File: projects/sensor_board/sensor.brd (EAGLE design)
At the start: 90.2 x 95.9 mm, 49 parts, among them J1 504050-0791, J2 FH28-10S-0.5SH_05_, J3 504050-0791, J4 504050-1091, J5 504050-0791, J6 504050-0791, U1 NXP_FXAS21002CQR1_EDITEDNXP_F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, U2 HONEYWELL_HMC5983-TRHONEYWELL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, U3 DS1307N, U4 NXP_FXAS21002CQR1_EDITEDNXP_F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, U5 HONEYWELL_HMC5983-TRHONEYWELL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, U6 NXP_FXAS21002CQR1_EDITEDNXP_F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, U7 HONEYWELL_HMC5983-TRHONEYWELL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, Y1 ECS-.327-12.5-13X

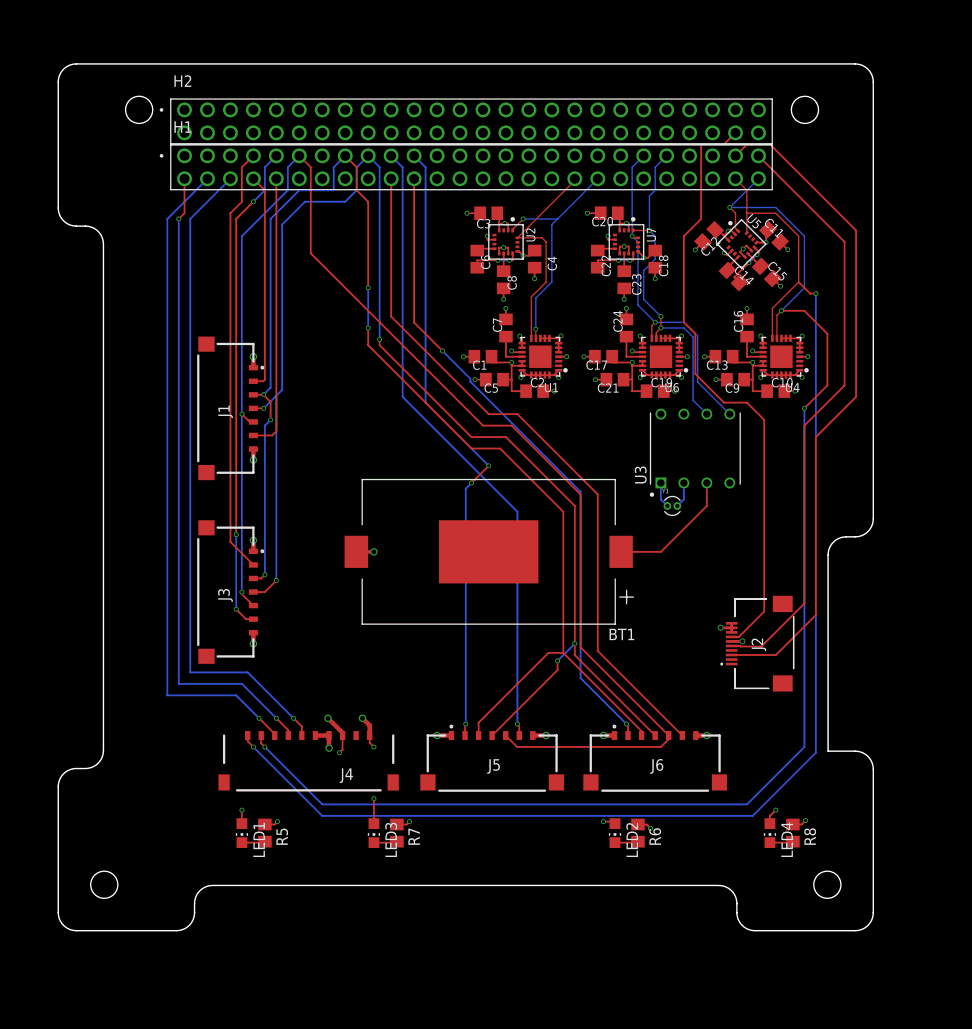
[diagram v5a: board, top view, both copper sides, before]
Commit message: sensor board updated
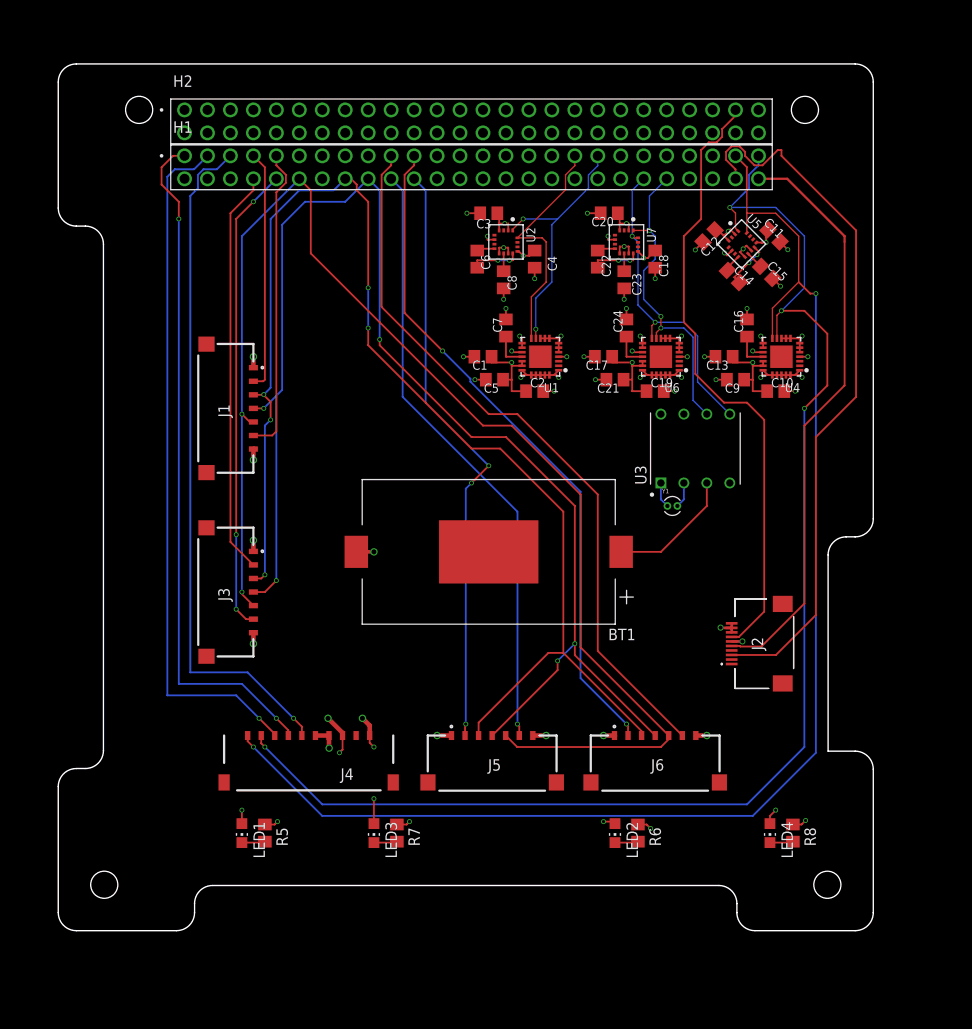
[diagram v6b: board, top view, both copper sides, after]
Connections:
- net 3V3_PDM10: now also H2.19; no longer H2.20
- net 3V3_PDM8: now also H2.17; no longer H2.18
- net 3V3_PDM9: now also H2.20; no longer H2.19
- net 5V_PDM5: now also H2.14; no longer H2.13
- net 5V_PDM6: now also H2.16; no longer H2.15
- net 5V_PDM7: now also H2.15; no longer H2.16
- net CHASSIS: now also H2.49; no longer H2.50
- net DTR: now also H1.5; no longer H1.6
- net GND: now also H2.10, H2.13, H2.18, H2.31; no longer H2.14, H2.17, H2.32, H2.9
- net I2C1_SCL: now also H1.44; no longer H1.43
- net I2C1_SDA: now also H1.42; no longer H1.41
- net I2C2_SCL: now also H1.37; no longer H1.38
- net I2C2_SDA: now also H1.35; no longer H1.36
- net I2C3_SCL: now also H1.51; no longer H1.52
- net I2C3_SDA: now also H1.49; no longer H1.50
- net SPI_EN_1: now also H1.7; no longer H1.8
- net SPI_EN_2: now also H1.8; no longer H1.7
- net SPI_EN_3: now also H1.22; no longer H1.21
- net SPI_EN_4: now also H1.21; no longer H1.22
- net SPI_MISO: now also H1.18; no longer H1.17
- net SPI_MOSI: now also H1.16; no longer H1.15
- net SPI_SCK: now also H1.12; no longer H1.11
- net SPI_SS_1: now also H1.9; no longer H1.10
- net SPI_SS_2: now also H1.10; no longer H1.9
- net SPI_SS_3: now also H1.20; no longer H1.19
- net SPI_SS_4: now also H1.19; no longer H1.20
- net UART2_RX: now also H1.4; no longer H1.3
- net UART2_TX: now also H1.2; no longer H1.1
- net UART3_RX: now also H1.52; no longer H1.51
- net UART3_TX: now also H1.50; no longer H1.49
- net UART8_RX: now also H1.3; no longer H1.4
- net UART8_TX: now also H1.1; no longer H1.2
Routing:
- net 3V3_PDM9: track 78.6 -> 104.5 mm
- net UART3_TX: track 73.3 -> 79.5 mm
- net SPI_MISO: track 153.4 -> 148.3 mm
- net SPI_SCK: track 156.8 -> 151.7 mm
- net UART8_TX: track 71.0 -> 75.8 mm
- net SPI_MOSI: track 149.0 -> 144.3 mm
- net UART8_RX: track 72.8 -> 76.6 mm
- net DTR: track 72.3 -> 75.7 mm
- net SPI_SS_1: track 30.7 -> 34.1 mm
- net SPI_SS_4: track 76.8 -> 80.2 mm
- net SPI_EN_4: track 71.4 -> 74.8 mm
- net 5V_PDM6: track 39.0 -> 41.8 mm
- net 5V_PDM7: track 21.0 -> 23.5 mm
- net SPI_EN_2: track 47.4 -> 44.8 mm
- net SPI_SS_3: track 70.0 -> 67.5 mm
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
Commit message: Update sensor.brd
Updated with fix to I2C lines
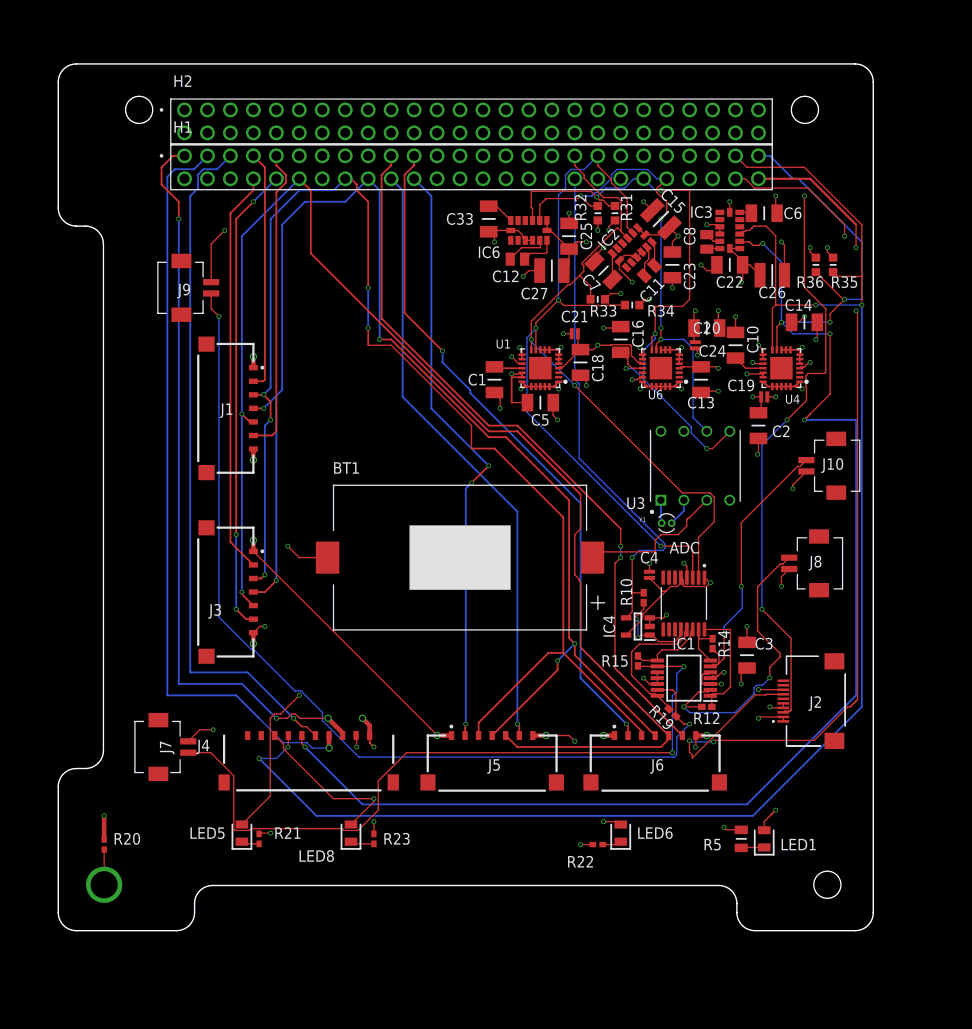
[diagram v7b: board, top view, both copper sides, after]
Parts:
- removed C17, C9: 1.0 uF, rcl:C0805
- removed LED2, LED3, LED4: (no value), led:CHIP-LED0805
- removed R6, R7, R8: (no value), rcl:R0805
- removed U2, U5, U7: HONEYWELL_HMC5983-TRHONEYWELL_HMC5983-TR_0_0, Honeywell - HMC5983-TR:HONEYWELL_HMC5983-TR_0
- added ADC: ADC128D818CIMT/NOPB, ADC128D818CIMT_NOPB:SOP65P640X120-16N
- added C25: C1206X104K5RAC3316, SamacSys_Parts:CAPC3316X98N
- added C26, C27: EMF325B7106KMHP, SamacSys_Parts:CAPC3225X270N
- added C33: C1206X475K3RACAUTO7210, SamacSys_Parts:CAPC3316X195N
- added IC1: TSX634AIYPT, SamacSys_Parts:SOP65P640X120-14N
- added IC2, IC3, IC6: LSM303DLHC, st-microelectronics:LGA-14
- added IC4: OPA991IDBVR, SamacSys_Parts:SOT95P280X145-5N
- added J10, J7, J8, J9: DF13A-2P-1.25H_21_, SamacSys_Parts:DF13A2P125H21
- added LED5, LED6, LED8: LG_R971-KN-1, SamacSys_Parts:LEDC2012X80N
- added R10, R12, R14, R15, R19: PTN0402Y1002BST1, SamacSys_Parts:RESC1106X84N
- added R20: PMR01ZZPJ000, SamacSys_Parts:RESC1005X35N
- added R21, R22, R23: CR0402-FX-1400GLF, SamacSys_Parts:RESC1005X40N
- added R31, R32, R33, R34, R35, R36: RS73G1JTTD4701B, SamacSys_Parts:RESC1608X55N
- BT1: device BA2032SM:BAT_BA2032SM -> BA2032SM_PAD_replace:BAT_BA2032SM
- C1: value 1.0 uF -> C1206X104K5RAC3316; device rcl:C0805 -> SamacSys_Parts:CAPC3316X98N
- C10, C13, C18, C2, C20, C3, C5: value 0.1 uF -> C1206X104K5RAC3316; device rcl:C0805 -> SamacSys_Parts:CAPC3316X98N
- C11, C12: value 0.1 uF -> C0805F224M5RACAUTO7210; device rcl:C0805 -> SamacSys_Parts:CAPC2012X140N
- C14, C22: value 0.22 uF -> C1206X104K5RAC3316; device rcl:C0805 -> SamacSys_Parts:CAPC3316X98N
- C15: value 4.7 uF -> EMF325B7106KMHP; device rcl:C0805 -> SamacSys_Parts:CAPC3225X270N
- C16: value 100 nF -> C1206X104K5RAC3316; device rcl:C0805 -> SamacSys_Parts:CAPC3316X98N
- C19, C21, C4: value 0.1 uF -> CGAEB1X7T0G105M050BC; device rcl:C0805 -> SamacSys_Parts:CAPC0611X68N
- C23: value 4.7 uF -> C1206X104K5RAC3316; device rcl:C0805 -> SamacSys_Parts:CAPC3316X98N
- C24: value 100 nF -> CGAEB1X7T0G105M050BC; device rcl:C0805 -> SamacSys_Parts:CAPC0611X68N
- C6: value 0.22 uF -> C1206X475K3RACAUTO7210; device rcl:C0805 -> SamacSys_Parts:CAPC3316X195N
- C7: value 100 nF -> C1206X475K3RACAUTO7210; device rcl:C0805 -> SamacSys_Parts:CAPC3316X195N
- C8: value 4.7 uF -> C0805F224M5RACAUTO7210; device rcl:C0805 -> SamacSys_Parts:CAPC2012X140N
- LED1: value (none) -> LH_R974-LP-1; device led:CHIP-LED0805 -> SamacSys_Parts:LEDC2012X90N
- R5: value (none) -> RN73H2ATTD75R0B25; device rcl:R0805 -> SamacSys_Parts:RESC2012X60N
- moved LED1 57.8 mm to (78.1, 10.2), turned to 90 degrees
- moved C3 56.6 mm to (76.2, 30.5), turned to 270 degrees
- moved R5 52.7 mm to (75.6, 10.2)
- moved C4 37.2 mm to (65.4, 39.4), turned to 90 degrees
- moved C6 32.2 mm to (78.1, 79.4), turned to 0 degrees
- moved C2 25.1 mm to (77.5, 55.9), turned to 270 degrees
- moved C8 22.9 mm to (71.8, 76.2)
- moved C12 21.4 mm to (50.8, 74.3), turned to 0 degrees
- moved C20 16.7 mm to (71.8, 66.7), turned to 0 degrees
- moved C22 14.6 mm to (74.3, 73.7), turned to 180 degrees
- moved C11 14.3 mm to (65.4, 73.0), turned to 45 degrees
- moved C18 14.1 mm to (57.8, 62.9)
- moved C16 14.0 mm to (62.2, 65.4)
- moved C15 13.1 mm to (66.7, 78.7), turned to 135 degrees
- moved C7 12.5 mm to (60.3, 73.0), turned to 135 degrees
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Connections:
- removed net N$45: C6.2, U2.12
- removed net N$46: C6.1, U2.8
- removed net N$47: C14.2, U5.12
- removed net N$48: C14.1, U5.8
- removed net N$49: C22.2, U7.12
- removed net N$50: C22.1, U7.8
- removed net N$51: C15.1, U5.10
- removed net N$52: C8.1, U2.10
- removed net N$56: C23.1, U7.10
- new net ADCIN0: ADC.16, IC1.1, R12.1
- new net ADCIN1: ADC.15, IC1.7, R14.1
- new net ADCIN2: ADC.14, IC1.8, R15.1
- new net ADCIN3: ADC.13, IC1.14, R19.1
- new net ADCIN4: ADC.12, IC4.1, R10.1
- new net CHASSIS_CONNECTION: R20.2
- new net N$10: C8.2, IC3.13
- new net N$11: C11.1, IC2.12
- new net N$12: C11.2, IC2.13
- new net N$13: C7.1, IC2.6
- new net N$14: C12.1, IC6.12
- new net N$15: C12.2, IC6.13
- new net N$16: C33.1, IC6.6
- new net N$8: C6.1, IC3.6
- new net N$9: C8.1, IC3.12
- new net PH1_POS: IC1.2, J8.1, R12.2
- new net PH2_POS: IC1.6, J10.1, R14.2
- new net PH3_POS: IC1.9, J7.1, R15.2
- new net PH4_POS: IC1.13, J9.1, R19.2
- new net PH5_POS: H1.36, IC4.4, R10.2
- net 3V3_PDM9: now also ADC.1, ADC.5, C14.1, C15.1, C19.2, C21.2, C22.1, C23.1, C24.2, C25.1, C26.1, C27.1, C3.2, IC1.4, IC2.1, IC2.14, IC3.1, IC3.14, IC4.5, IC6.1, IC6.14, J2.1, J2.2, LED1.2, R31.2, R32.2, R33.2, R34.2, R35.2, R36.2; no longer C1.1, C10.1, C11.1, C12.1, C17.1, C19.1, C21.1, C3.1, C9.1, J2.6, LED4.A, U2.13, U2.2, U2.4, U2.6, U5.13, U5.2, U5.4, U5.6, U7.13, U7.2, U7.4, U7.6
- net 5V_PDM5: now also LED5.2; no longer J4.3, LED1.A
- net 5V_PDM6: now also LED6.2; no longer LED2.A
- net 5V_PDM7: now also J4.8, LED8.2; no longer LED3.A
- net CHASSIS: now also J2.3; no longer J2.7
- net DTR: now also J4.5; no longer J4.6
- net GND: now also ADC.4, C14.2, C19.1, C21.1, C22.2, C24.1, C25.2, C26.2, C27.2, C3.1, C33.2, C6.2, H1.38, IC1.10, IC1.11, IC1.12, IC1.3, IC1.5, IC2.10, IC2.11, IC2.7, IC3.10, IC3.11, IC3.7, IC4.2, IC4.3, IC6.10, IC6.11, IC6.7, J10.2, J2.4, J2.5, J4.2, J7.2, J8.2, J9.2, R20.1, R21.1, R22.1, R23.1; no longer C11.2, C12.2, C17.2, C19.2, C21.2, C24.2, C3.2, C8.2, C9.2, J2.10, J2.8, J2.9, J4.4, J4.5, R6.1, R7.1, R8.1, U2.11, U2.9, U5.11, U5.9, U7.11, U7.9
- net I2C1_SCL: now also IC6.2, R32.1; no longer U7.1
- net I2C1_SDA: now also IC6.3, R31.1; no longer U7.16
- net I2C2_SCL: now also ADC.3, IC2.2, R34.1; no longer U2.1
- net I2C2_SDA: now also ADC.2, IC2.3, R33.1; no longer U2.16
- net I2C3_SCL: now also IC3.2, J4.6, R36.1; no longer J4.9, U5.1
- net I2C3_SDA: now also IC3.3, J4.7, R35.1; no longer J4.10, U5.16
- net N$1: now also LED5.1, R21.2; no longer LED1.C, R5.2
- net N$2: now also LED6.1, R22.2; no longer LED2.C, R6.2
- net N$3: now also LED8.1, R23.2; no longer LED3.C, R7.2
- net N$4: now also LED1.1, R5.2; no longer LED4.C, R8.2
- net N$67: now also C10.1; no longer C16.1
- net N$71: now also C1.1; no longer C7.1
- net N$72: now also C16.1; no longer C24.1
- net UART3_RX: now also J2.7; no longer J2.5
- net UART3_TX: now also J2.8; no longer J2.3
- net UART8_RX: now also J4.4; no longer J4.8
- net UART8_TX: now also J4.3; no longer J4.7
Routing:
- net PH4_POS: track 0.00 -> 104.5 mm, vias 0 -> 2
- net PH3_POS: track 0.00 -> 81.4 mm, vias 0 -> 2
- net 5V_PDM6: track 41.8 -> 118.1 mm
- net PH5_POS: track 0.00 -> 57.3 mm, vias 0 -> 1
- net GND: track 86.3 -> 142.9 mm, vias 47 -> 60
- net I2C2_SCL: track 28.6 -> 80.3 mm, vias 2 -> 3
- net I2C2_SDA: track 26.4 -> 71.1 mm, vias 0 -> 2
- net UART3_RX: track 64.7 -> 101.1 mm, vias 0 -> 4
- net 3V3_PDM9: track 104.5 -> 140.8 mm, vias 20 -> 25
- net PH1_POS: track 0.00 -> 33.9 mm, vias 0 -> 2
- net I2C1_SDA: track 35.5 -> 67.9 mm, vias 2 -> 5
- net PH2_POS: track 0.00 -> 29.7 mm, vias 0 -> 2
- net I2C3_SDA: track 151.4 -> 180.2 mm, vias 2 -> 4
- net I2C3_SCL: track 151.5 -> 175.1 mm, vias 4 -> 7
- net I2C1_SCL: track 35.1 -> 54.5 mm, vias 3 -> 4
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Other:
- outline, holes or cut-outs redrawn
